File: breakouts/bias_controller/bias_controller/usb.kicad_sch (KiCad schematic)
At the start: 34 parts, among them J1 USB_C_Receptacle_USB2.0, Q1 AO4407, Q2 AO3400A, U2 LDR6321

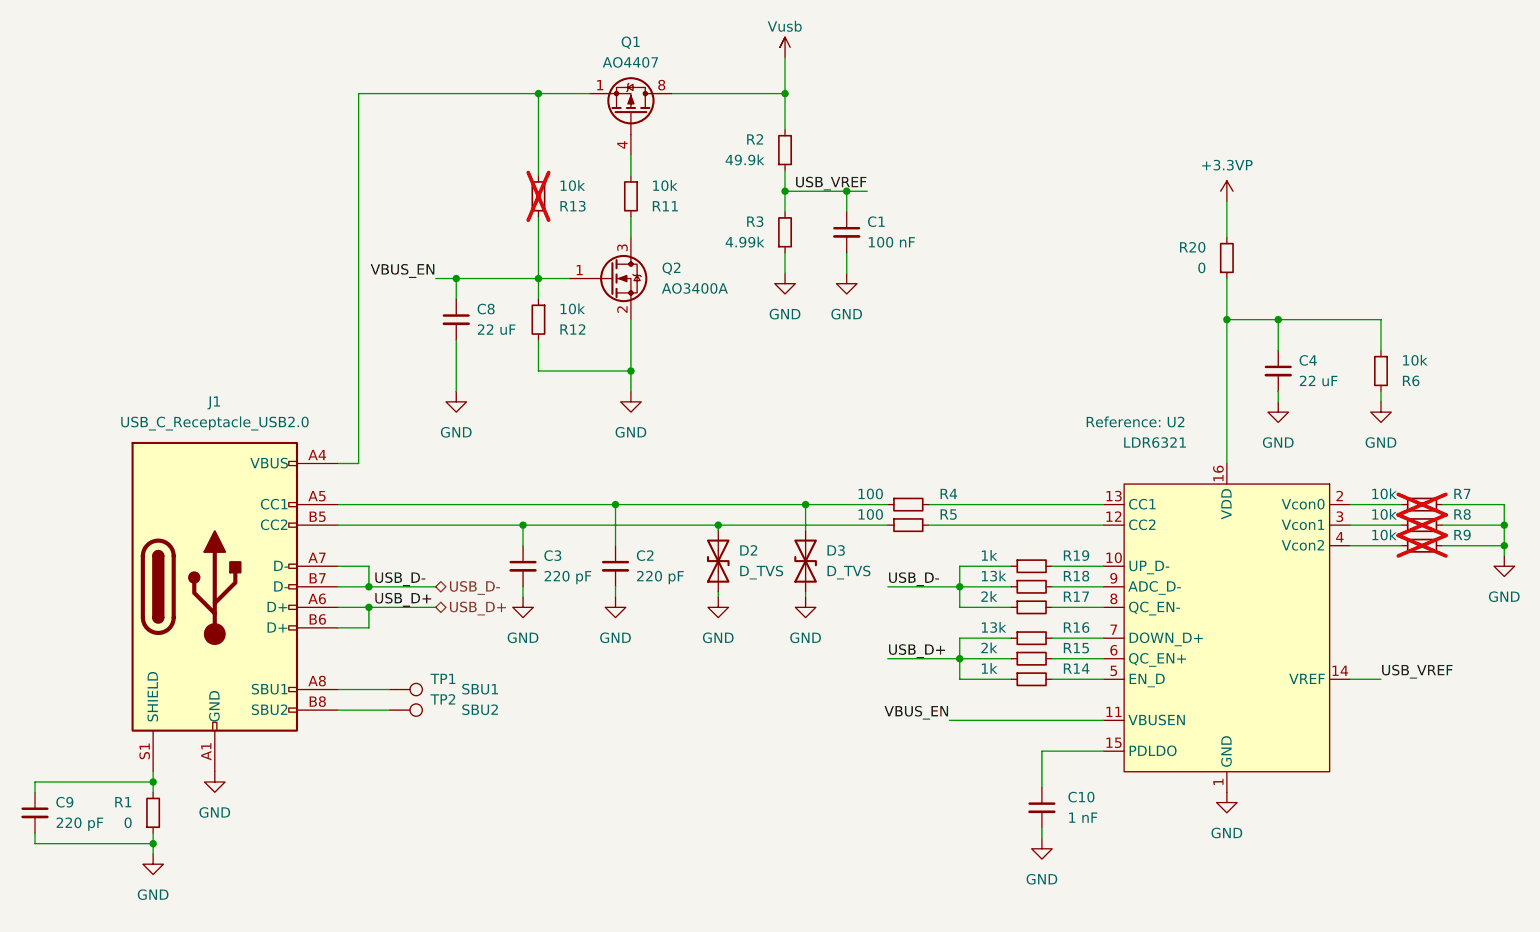
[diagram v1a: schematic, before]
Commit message: bias controller schematic cleanup
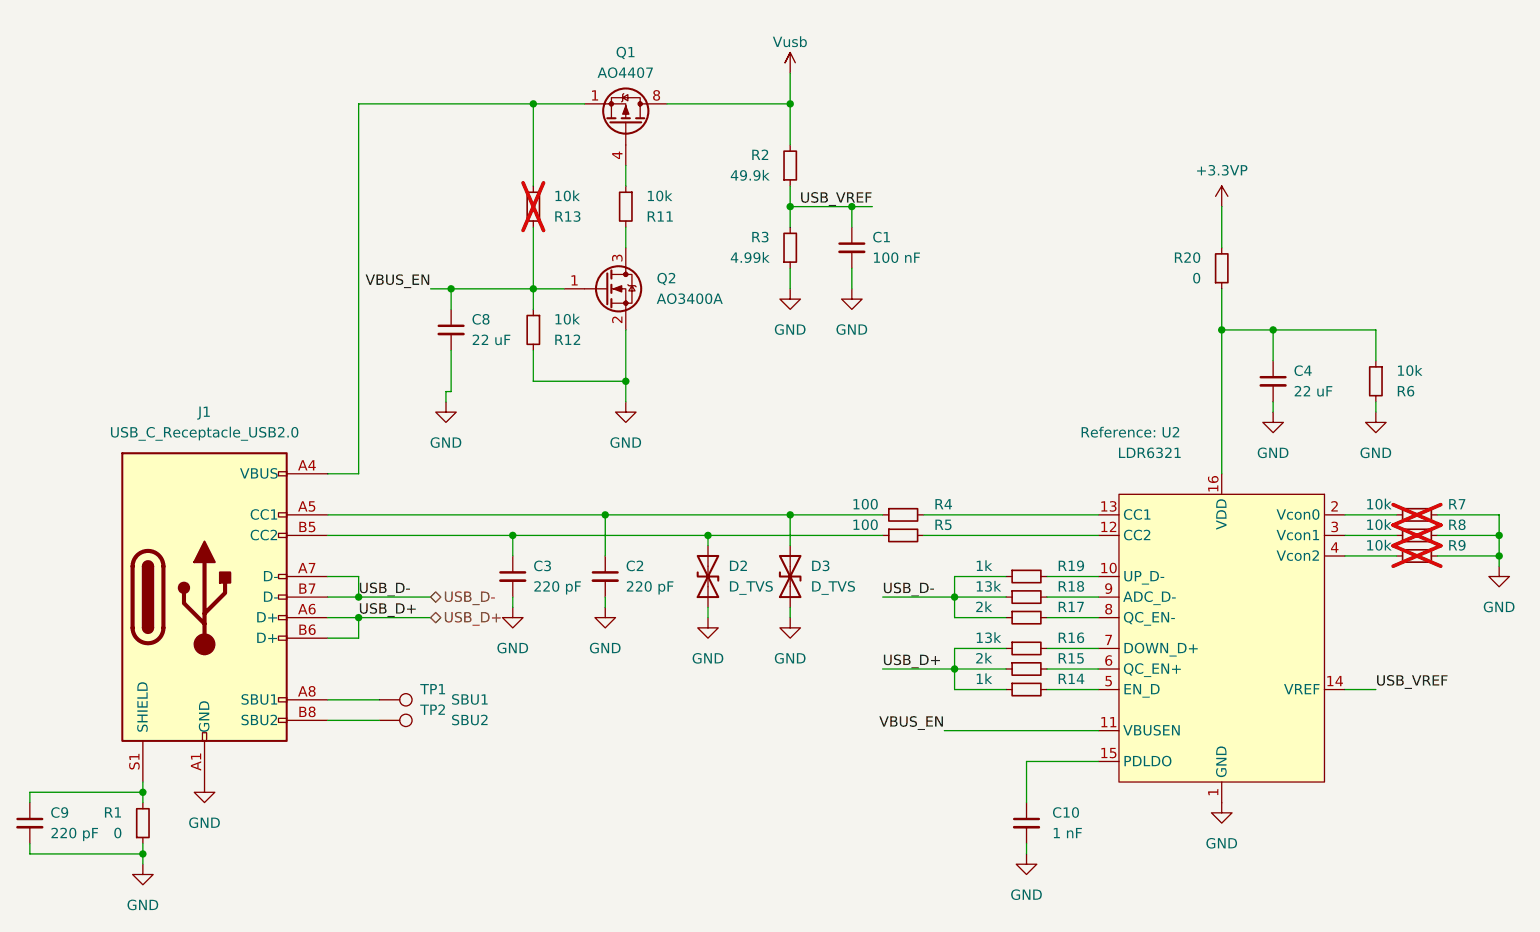
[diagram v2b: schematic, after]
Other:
- moved on the sheet: C1, C10, C2, C4, C8, C9, D2, D3, J1, Q1, Q2, R1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

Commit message: most footprint assignments on bias controller board, schematic cleanup
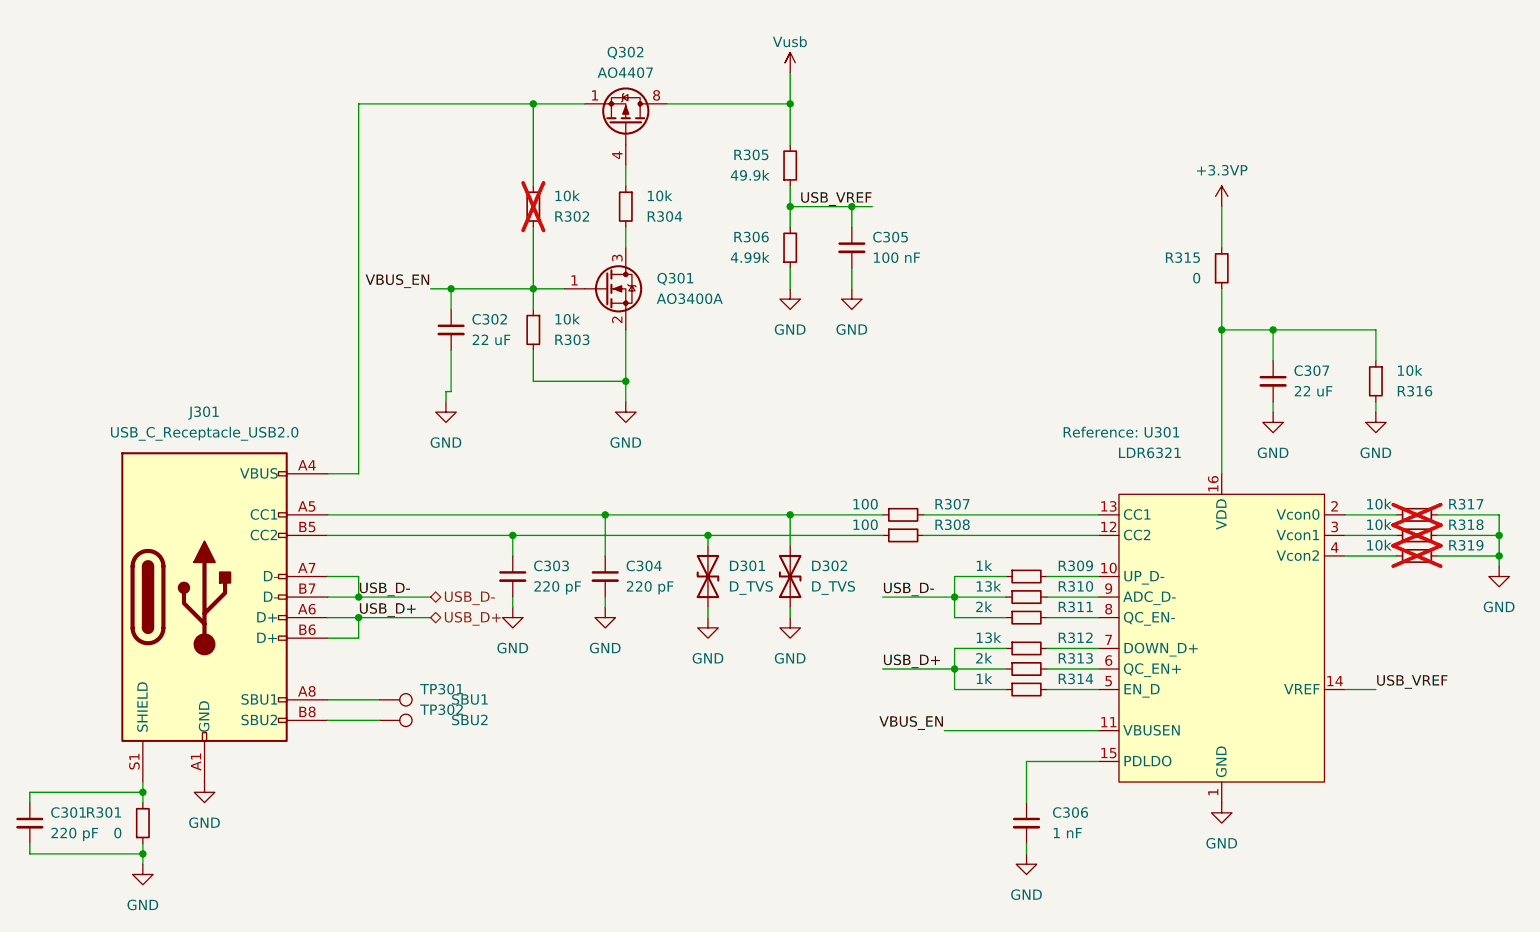
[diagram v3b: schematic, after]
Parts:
- C301: renamed from C9; footprint (none) -> Capacitor_SMD:C_0402_1005Metric
- C302: renamed from C8; footprint (none) -> Capacitor_SMD:C_0805_2012Metric
- C303: renamed from C3; footprint (none) -> Capacitor_SMD:C_0402_1005Metric
- C304: renamed from C2; footprint (none) -> Capacitor_SMD:C_0402_1005Metric
- C305: renamed from C1; footprint (none) -> Capacitor_SMD:C_0402_1005Metric
- C306: renamed from C10; footprint (none) -> Capacitor_SMD:C_0402_1005Metric
- C307: renamed from C4; footprint (none) -> Capacitor_SMD:C_0603_1608Metric
- R301: renamed from R1; footprint (none) -> Resistor_SMD:R_0402_1005Metric
- R302: renamed from R13; footprint (none) -> Resistor_SMD:R_0402_1005Metric
- R303: renamed from R12; footprint (none) -> Resistor_SMD:R_0402_1005Metric
- R304: renamed from R11; footprint (none) -> Resistor_SMD:R_0402_1005Metric
- R305: renamed from R2; footprint (none) -> Resistor_SMD:R_0402_1005Metric
- R306: renamed from R3; footprint (none) -> Resistor_SMD:R_0402_1005Metric
- R307: renamed from R4; footprint (none) -> Resistor_SMD:R_0402_1005Metric
- R308: renamed from R5; footprint (none) -> Resistor_SMD:R_0402_1005Metric
- R309: renamed from R19; footprint (none) -> Resistor_SMD:R_0402_1005Metric
- R310: renamed from R18; footprint (none) -> Resistor_SMD:R_0402_1005Metric
- R311: renamed from R17; footprint (none) -> Resistor_SMD:R_0402_1005Metric
- R312: renamed from R16; footprint (none) -> Resistor_SMD:R_0402_1005Metric
- R313: renamed from R15; footprint (none) -> Resistor_SMD:R_0402_1005Metric
- R314: renamed from R14; footprint (none) -> Resistor_SMD:R_0402_1005Metric
- R315: renamed from R20; footprint (none) -> Resistor_SMD:R_0402_1005Metric
- R316: renamed from R6; footprint (none) -> Resistor_SMD:R_0402_1005Metric
- R317: renamed from R7; footprint (none) -> Resistor_SMD:R_0402_1005Metric
- R318: renamed from R8; footprint (none) -> Resistor_SMD:R_0402_1005Metric
- R319: renamed from R9; footprint (none) -> Resistor_SMD:R_0402_1005Metric
- TP301: renamed from TP1; footprint (none) -> TestPoint:TestPoint_Pad_D1.0mm
- TP302: renamed from TP2; footprint (none) -> TestPoint:TestPoint_Pad_D1.0mm
- renumbered D2 to D301, D3 to D302, J1 to J301, Q2 to Q301, Q1 to Q302, U2 to U301

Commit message: schematic and footprint assignment cleanup
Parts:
- D301, D302: value D_TVS -> ESD9B5VL; footprint (none) -> jtk_rf_footprints:DFN1006-2
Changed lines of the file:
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@@
 	(wire
 		(pts
-			(xy 79.375 77.47) (xy 79.375 78.74)
+			(xy 80.01 72.39) (xy 80.01 80.01)
 		)
 		(stroke
@@
 	(wire
 		(pts
-			(xy 79.375 77.47) (xy 80.01 77.47)
-		)
-		(stroke
-			(width 0)
-			(type default)
-		)
-	)
-	(wire
-		(pts
 			(xy 68.58 41.91) (xy 68.58 87.63)
 		)
@@
 	(wire
 		(pts
-			(xy 80.01 77.47) (xy 80.01 72.39)
-		)
-		(stroke
-			(width 0)
-			(type default)
-		)
-	)
-	(wire
-		(pts
 			(xy 64.77 115.57) (xy 71.12 115.57)
 		)
@@
 	(symbol
 		(lib_id "power:GND")
-		(at 79.375 78.74 0)
+		(at 80.01 80.01 0)
 		(mirror y)
 		(unit 1)
@@
 		(fields_autoplaced yes)
 		(property "Reference" "#PWR0303"
-			(at 79.375 85.09 0)
+			(at 80.01 86.36 0)
 			(effects
 				(font
@@
 		)
 		(property "Value" "GND"
-			(at 79.375 83.82 0)
+			(at 80.01 85.09 0)
 			(effects
 				(font
@@
 		)
 		(property "Footprint" ""
-			(at 79.375 78.74 0)
+			(at 80.01 80.01 0)
 			(effects
 				(font
@@
 		)
 		(property "Datasheet" ""
-			(at 79.375 78.74 0)
+			(at 80.01 80.01 0)
 			(effects
 				(font
@@
 		)
 		(property "Description" ""
-			(at 79.375 78.74 0)
+			(at 80.01 80.01 0)
 			(effects
 				(font
@@
 		(on_board yes)
 		(dnp no)
-		(fields_autoplaced yes)
 		(property "Reference" "D301"
-			(at 114.3 99.06 90)
+			(at 114.3 99.0599 90)
 			(effects
 				(font
@@
 			)
 		)
-		(property "Value" "D_TVS"
-			(at 114.3 101.6 90)
+		(property "Value" "ESD9B5VL"
+			(at 112.014 104.902 90)
 			(effects
 				(font
@@
 			)
 		)
-		(property "Footprint" ""
+		(property "Footprint" "jtk_rf_footprints:DFN1006-2"
 			(at 111.76 100.33 0)
 			(effects
@@
 		(on_board yes)
 		(dnp no)
-		(fields_autoplaced yes)
 		(property "Reference" "D302"
-			(at 124.46 99.06 90)
+			(at 124.46 99.0599 90)
 			(effects
 				(font
@@
 			)
 		)
-		(property "Value" "D_TVS"
-			(at 124.46 101.6 90)
+		(property "Value" "ESD9B5VL"
+			(at 123.698 104.648 90)
 			(effects
 				(font
@@
 			)
 		)
-		(property "Footprint" ""
+		(property "Footprint" "jtk_rf_footprints:DFN1006-2"
 			(at 121.92 100.33 0)
 			(effects

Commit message: added LCSC part numbers to all components on bias board
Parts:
- C301, C303, C304: LCSC Part # (none) -> C1530
- C302: LCSC Part # (none) -> C45783
- C305: LCSC Part # (none) -> C307331
- C306: LCSC Part # (none) -> C1523
- C307: footprint Capacitor_SMD:C_0603_1608Metric -> Capacitor_SMD:C_0805_2012Metric; LCSC Part # (none) -> C45783
- D301, D302: LCSC Part # (none) -> C2827544
- J301: LCSC Part # (none) -> C2988369
- Q301: LCSC Part # (none) -> C20917
- Q302: LCSC Part # (none) -> C5370947
- R301, R315: LCSC Part # (none) -> C17168
- R302, R303, R304, R316, R317, R318, R319: LCSC Part # (none) -> C25744
- R305: value 49.9k -> 51k; LCSC Part # (none) -> C25794
- R306: value 4.99k -> 51k; LCSC Part # (none) -> C25794
- R307, R308: LCSC Part # (none) -> C25076
- R309, R314: LCSC Part # (none) -> C11702
- R310, R312: value 13k -> 12k; LCSC Part # (none) -> C25752
- R311, R313: LCSC Part # (none) -> C4109
- TP301, TP302: LCSC Part # (none) -> DNI; now left out of the parts list
- U301: LCSC Part # (none) -> C2919632
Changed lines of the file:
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@@
 			)
 		)
-		(property "LCSC Part #" ""
+		(property "LCSC Part #" "C4109"
 			(at 151.13 105.41 0)
 			(effects
@@
 			)
 		)
-		(property "LCSC Part #" ""
+		(property "LCSC Part #" "C25076"
 			(at 135.89 95.25 0)
 			(effects
@@
 			)
 		)
-		(property "Value" "13k"
+		(property "Value" "12k"
 			(at 144.78 107.95 90)
 			(effects
@@
 			)
 		)
-		(property "LCSC Part #" ""
+		(property "LCSC Part #" "C25752"
 			(at 151.13 109.22 0)
 			(effects
@@
 			)
 		)
-		(property "LCSC Part #" ""
+		(property "LCSC Part #" "C25744"
 			(at 90.17 69.85 0)
 			(effects
@@
 			)
 		)
-		(property "LCSC Part #" ""
+		(property "LCSC Part #" "C2919632"
 			(at 175.26 107.95 0)
 			(effects
@@
 			)
 		)
-		(property "LCSC Part #" ""
+		(property "LCSC Part #" "C4109"
 			(at 151.13 111.76 0)
 			(effects
@@
 			)
 		)
-		(property "LCSC Part #" ""
+		(property "LCSC Part #" "C1523"
 			(at 151.13 130.81 0)
 			(effects
@@
 		(unit 1)
 		(exclude_from_sim no)
-		(in_bom yes)
+		(in_bom no)
 		(on_board yes)
 		(dnp no)
@@
 			)
 		)
-		(property "LCSC Part #" ""
+		(property "LCSC Part #" "DNI"
 			(at 71.12 118.11 0)
 			(effects
@@
 			)
 		)
-		(property "Value" "49.9k"
+		(property "Value" "51k"
 			(at 119.38 50.8 0)
 			(effects
@@
 			)
 		)
-		(property "LCSC Part #" ""
+		(property "LCSC Part #" "C25794"
 			(at 121.92 49.53 0)
 			(effects
@@
 			)
 		)
-		(property "LCSC Part #" ""
+		(property "LCSC Part #" "C25744"
 			(at 101.6 54.61 0)
 			(effects
@@
 			)
 		)
-		(property "LCSC Part #" ""
+		(property "LCSC Part #" "C1530"
 			(at 99.06 100.33 0)
 			(effects
@@
 			)
 		)
-		(property "LCSC Part #" ""
+		(property "LCSC Part #" "C25744"
 			(at 199.39 95.25 0)
 			(effects
@@
 			)
 		)
-		(property "Value" "4.99k"
+		(property "Value" "51k"
 			(at 119.38 60.96 0)
 			(effects
@@
 			)
 		)
-		(property "LCSC Part #" ""
+		(property "LCSC Part #" "C25794"
 			(at 121.92 59.69 0)
 			(effects
@@
 			)
 		)
-		(property "Value" "13k"
+		(property "Value" "12k"
 			(at 144.78 101.6 90)
 			(effects
@@
 			)
 		)
-		(property "LCSC Part #" ""
+		(property "LCSC Part #" "C25752"
 			(at 151.13 102.87 0)
 			(effects
@@
 			)
 		)
-		(property "LCSC Part #" ""
+		(property "LCSC Part #" "C25076"
 			(at 135.89 92.71 0)
 			(effects
@@
 			)
 		)
-		(property "LCSC Part #" ""
+		(property "LCSC Part #" "C1530"
 			(at 87.63 100.33 0)
 			(effects
@@
 			)
 		)
-		(property "LCSC Part #" ""
+		(property "LCSC Part #" "C25744"
 			(at 90.17 54.61 0)
 			(effects
@@
 			)
 		)
-		(property "Footprint" "Capacitor_SMD:C_0603_1608Metric"
+		(property "Footprint" "Capacitor_SMD:C_0805_2012Metric"
 			(at 181.61 76.2 0)
 			(effects
@@
 			)
 		)
-		(property "LCSC Part #" ""
+		(property "LCSC Part #" "C45783"
 			(at 181.61 76.2 0)
 			(effects
@@
 			)
 		)
-		(property "LCSC Part #" ""
+		(property "LCSC Part #" "C17168"
 			(at 175.26 62.23 0)
 			(effects
@@
 			)
 		)
-		(property "LCSC Part #" ""
+		(property "LCSC Part #" "C5370947"
 			(at 101.6 44.45 0)
 			(effects
@@
 			)
 		)
-		(property "LCSC Part #" ""
+		(property "LCSC Part #" "C2827544"
 			(at 111.76 100.33 0)
 			(effects
@@
 			)
 		)
-		(property "LCSC Part #" ""
+		(property "LCSC Part #" "C25744"
 			(at 199.39 97.79 0)
 			(effects
@@
 			)
 		)
-		(property "LCSC Part #" ""
+		(property "LCSC Part #" "C11702"
 			(at 151.13 114.3 0)
 			(effects
@@
 			)
 		)
-		(property "LCSC Part #" ""
+		(property "LCSC Part #" "C1530"
 			(at 27.94 130.81 0)
 			(effects
@@
 			)
 		)
-		(property "LCSC Part #" ""
+		(property "LCSC Part #" "C17168"
 			(at 41.91 130.81 0)
 			(effects
@@
 			)
 		)
-		(property "LCSC Part #" ""
+		(property "LCSC Part #" "C20917"
 			(at 99.06 64.77 0)
 			(effects
@@
 			)
 		)
-		(property "LCSC Part #" ""
+		(property "LCSC Part #" "C2988369"
 			(at 49.53 102.87 0)
 			(effects
@@
 			)
 		)
-		(property "LCSC Part #" ""
+		(property "LCSC Part #" "C25744"
 			(at 199.39 92.71 0)
 			(effects
@@
 			)
 		)
-		(property "LCSC Part #" ""
+		(property "LCSC Part #" "C45783"
 			(at 80.01 69.85 0)
 			(effects
@@
 			)
 		)
-		(property "LCSC Part #" ""
+		(property "LCSC Part #" "C307331"
 			(at 129.54 59.69 0)
 			(effects
@@
 			)
 		)
-		(property "LCSC Part #" ""
+		(property "LCSC Part #" "C2827544"
 			(at 121.92 100.33 0)
 			(effects
@@
 			)
 		)
-		(property "LCSC Part #" ""
+		(property "LCSC Part #" "C11702"
 			(at 151.13 100.33 0)
 			(effects
@@
 		(unit 1)
 		(exclude_from_sim no)
-		(in_bom yes)
+		(in_bom no)
 		(on_board yes)
 		(dnp no)
@@
 			)
 		)
-		(property "LCSC Part #" ""
+		(property "LCSC Part #" "DNI"
 			(at 71.12 115.57 0)
 			(effects
@@
 			)
 		)
-		(property "LCSC Part #" ""
+		(property "LCSC Part #" "C25744"
 			(at 194.31 76.2 0)
 			(effects
